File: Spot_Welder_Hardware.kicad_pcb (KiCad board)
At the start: 2 copper layers, 256.5 x 182.9 mm, 151 parts, among them J1 Mini USB, J2 Conn_01x03_Male, Q1 Q_NMOS_GSD, Q10 Q_NMOS_GDS, Q11 Q_NMOS_GDS, Q12 Q_NMOS_GDS, Q13 Q_NMOS_GDS, Q2 2N2219, Q3 Q_NMOS_GDS, Q4 Q_NMOS_GDS, Q5 Q_NMOS_GDS, Q6 Q_NMOS_GDS, Q7 Q_NMOS_GDS, Q8 Q_NMOS_GDS, Q9 Q_NMOS_GDS, SW1 SW_Push, SW2 SW_SPDT, SW3 Lead Voltage Trigger, SW4 SW_Push, U1 OKI, U2 ATMEGA328P, U3 FAN3122TMXCT-ND, U4 FT232RL, U5 FAN3122TMXCT-ND, Y1 Crystal

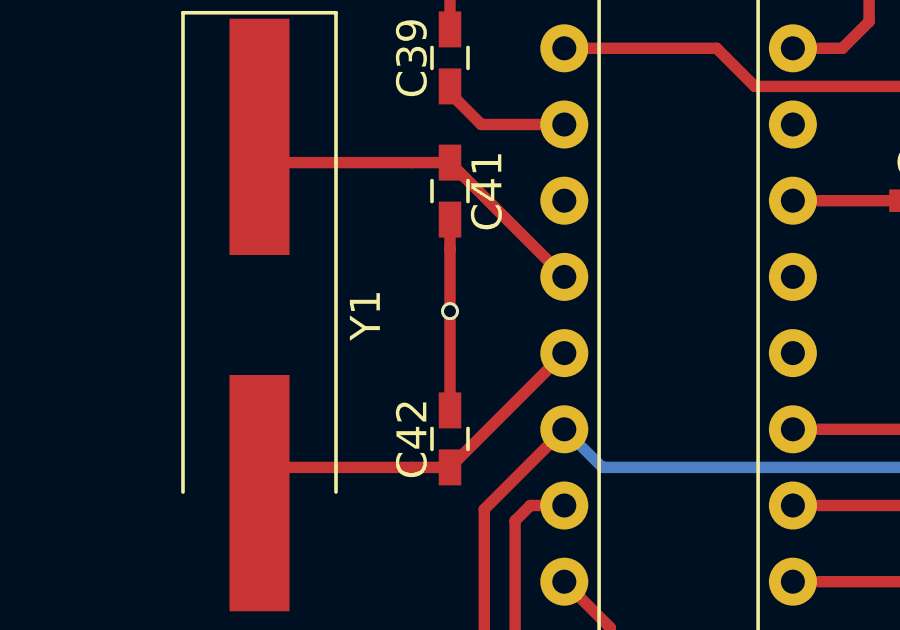
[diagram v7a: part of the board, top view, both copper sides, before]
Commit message: Fixed Vias on crystal caps
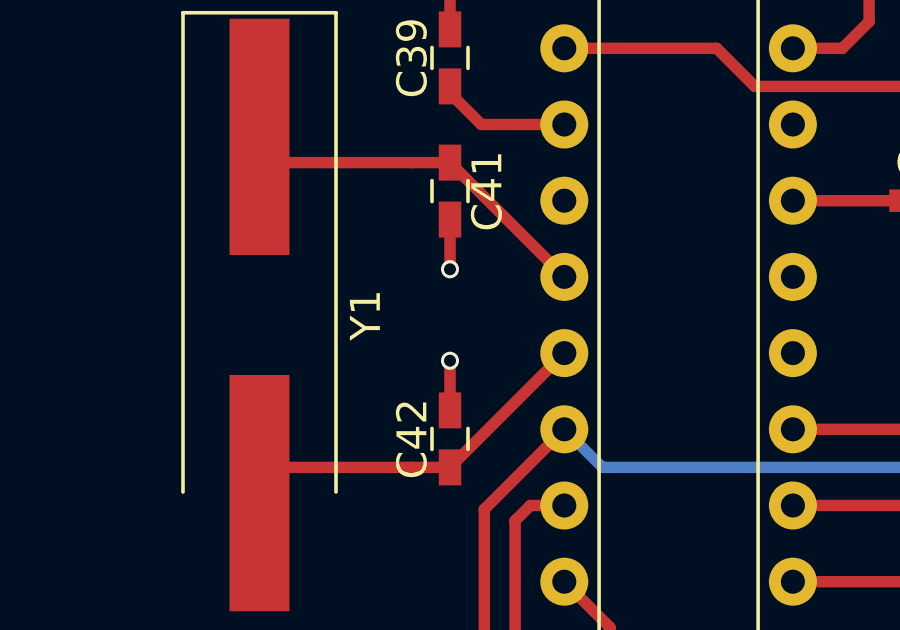
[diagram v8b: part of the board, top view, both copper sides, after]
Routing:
- net GND: track 178.6 -> 175.5 mm, vias 39 -> 40
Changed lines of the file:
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@@
   )
   (setup
-    (last_trace_width 0.25)
+    (last_trace_width 0.381)
     (user_trace_width 0.254)
     (user_trace_width 0.381)
@@
   (segment (start -39.116 32.512) (end -39.116 33.66) (width 0.381) (layer F.Cu) (net 4))
   (segment (start -39.116 31.11) (end -39.116 32.512) (width 0.381) (layer F.Cu) (net 4))
-  (segment (start 0 56.221) (end 0 58.293) (width 0.381) (layer F.Cu) (net 4))
-  (segment (start 0 55.24) (end 0 56.221) (width 0.381) (layer F.Cu) (net 4))
-  (segment (start 0 58.293) (end 0 61.6) (width 0.381) (layer F.Cu) (net 4))
-  (via (at 0 58.293) (size 0.6) (drill 0.4) (layers F.Cu B.Cu) (net 4))
   (via (at 0 46.736) (size 0.6) (drill 0.4) (layers F.Cu B.Cu) (net 4))
   (segment (start 0 48.9) (end 0 46.736) (width 0.381) (layer F.Cu) (net 4))
@@
   (segment (start -31.664 15.326) (end -35.56 11.43) (width 1.27) (layer F.Cu) (net 4))
   (segment (start -31.664 29.718) (end -31.664 15.326) (width 1.27) (layer F.Cu) (net 4))
+  (via (at 0 56.896) (size 0.6) (drill 0.4) (layers F.Cu B.Cu) (net 4))
+  (segment (start 0 55.24) (end 0 56.896) (width 0.381) (layer F.Cu) (net 4))
+  (via (at 0 59.944) (size 0.6) (drill 0.4) (layers F.Cu B.Cu) (net 4))
+  (segment (start 0 61.6) (end 0 59.944) (width 0.381) (layer F.Cu) (net 4))
   (segment (start 11.43 54.61) (end 15.24 54.61) (width 0.381) (layer F.Cu) (net 5))
   (segment (start 0 53.34) (end 3.81 57.15) (width 0.381) (layer F.Cu) (net 6))
